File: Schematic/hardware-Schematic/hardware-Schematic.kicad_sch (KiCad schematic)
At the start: 22 parts, among them J1 DC 5V Input, Q1 NDP6020P, U1 ATmega328P-P, U14 YP-05, U16 DFPlayer, U17 MP1584, U2 HW-084

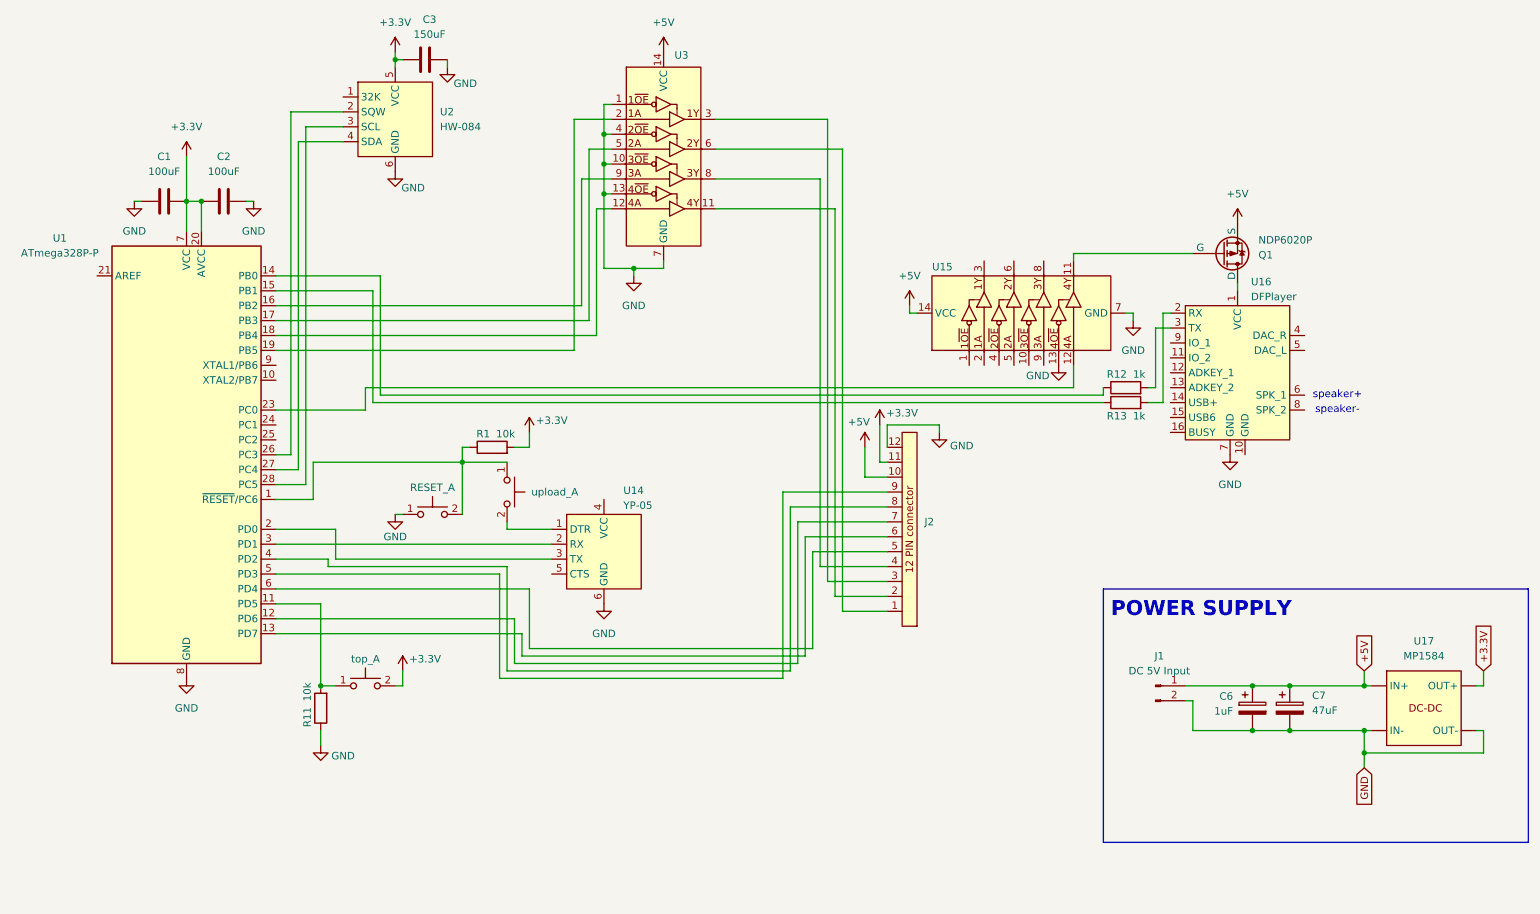
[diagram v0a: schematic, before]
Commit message: Making the hardware schematic ready for PCB implementation
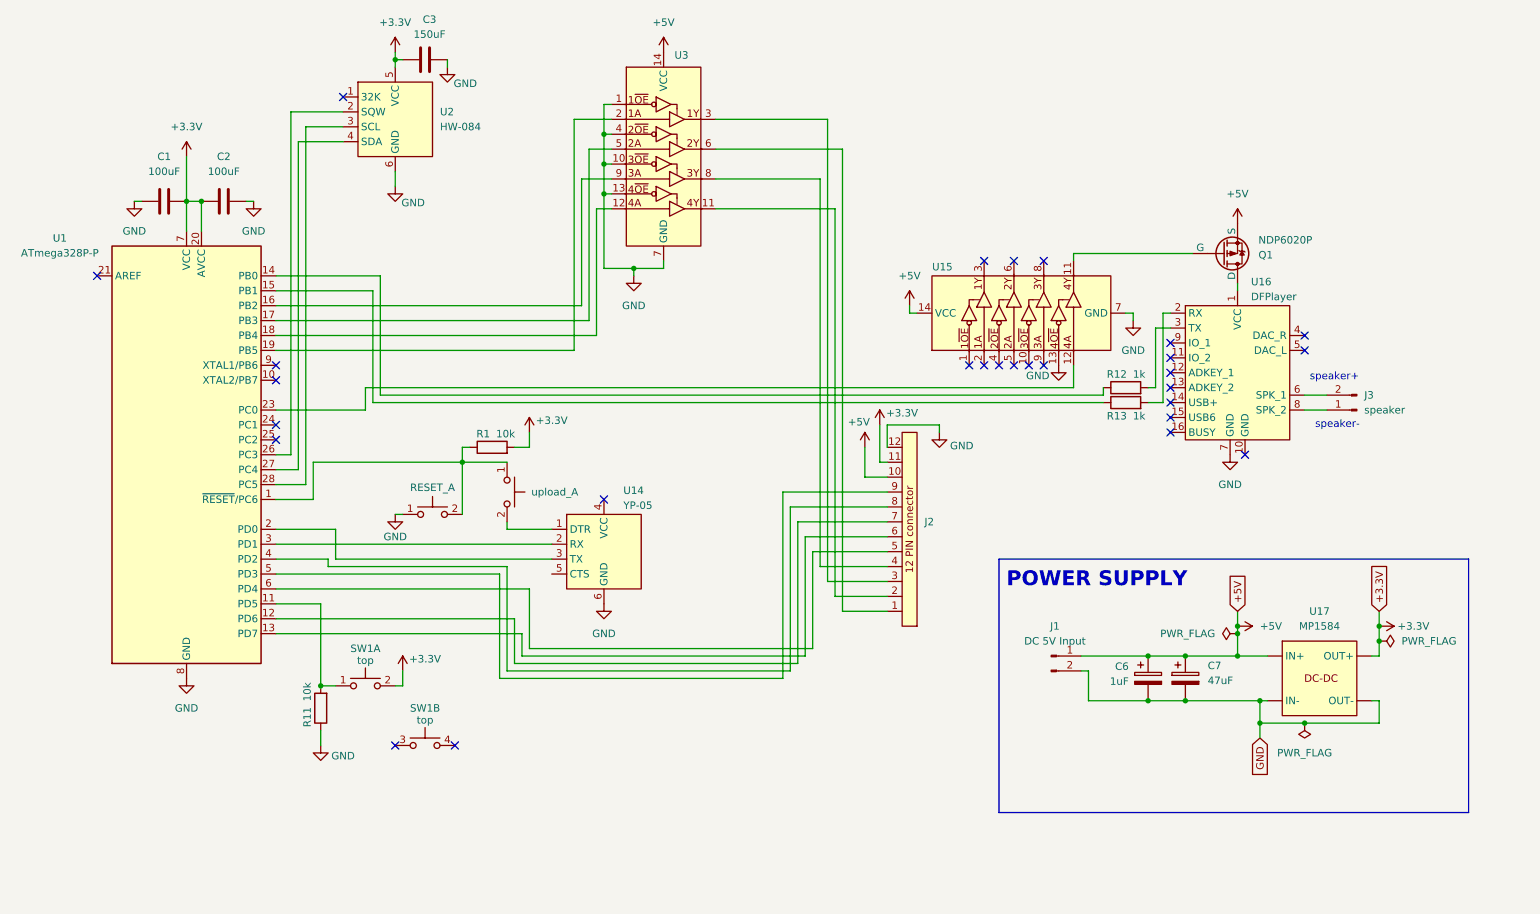
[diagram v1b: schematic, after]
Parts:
- removed top_: SW_Push_Dual_x2, symbol Switch:SW_Push_Dual_x2
- added J3: speaker, symbol Connector:Conn_01x02_Pin
- added SW1: top, symbol Switch:SW_Push_Dual_x2
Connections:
- net +3.3V: now also SW1.2 (D)
- net at U16.6 (SPK_1): now also J3.2 (Pin_2)
- net at U16.8 (SPK_2): now also J3.1 (Pin_1)
- net at R11.2, U1.11 (PD5): now also SW1.1 (C)
- no-connect marks 0 -> 28
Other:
- moved on the sheet: C6, C7, J1, U17

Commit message: USC-C to 5V DC plug added to custom lib
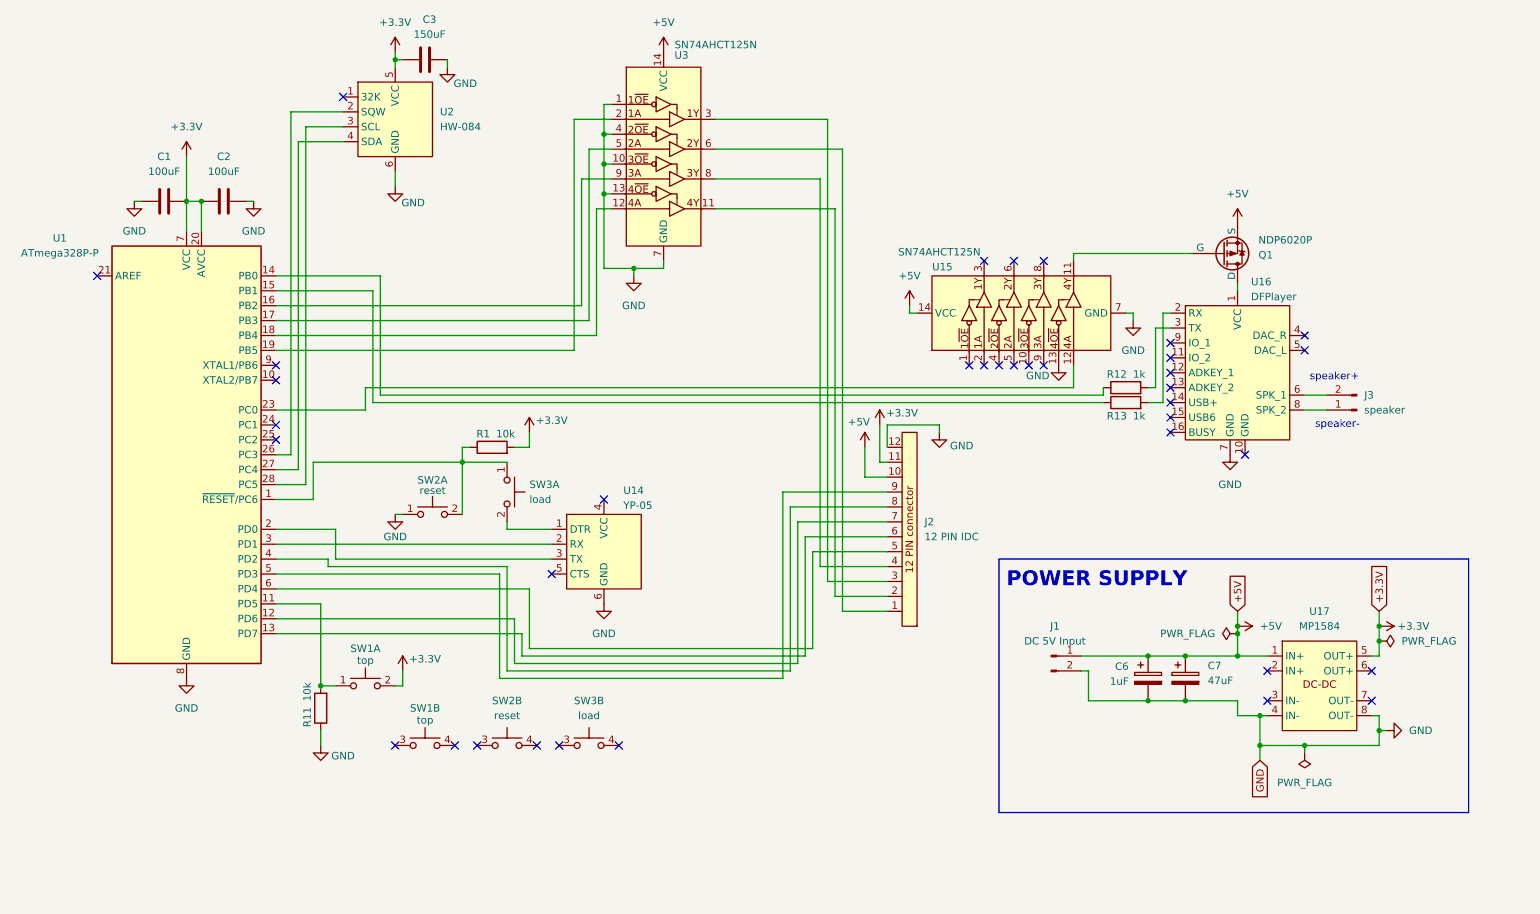
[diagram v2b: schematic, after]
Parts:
- removed RESET_, upload_: SW_Push_Dual_x2, symbol Switch:SW_Push_Dual_x2
- added SW2: reset, symbol Switch:SW_Push_Dual_x2
- added SW3: load, symbol Switch:SW_Push_Dual_x2
- C1, C2: footprint (none) -> Capacitor_THT:C_Axial_L12.0mm_D6.5mm_P15.00mm_Horizontal
- C3: footprint (none) -> Capacitor_THT:C_Rect_L7.2mm_W3.0mm_P5.00mm_FKS2_FKP2_MKS2_MKP2
- C6, C7: footprint (none) -> Capacitor_THT:CP_Radial_D5.0mm_P2.50mm
- J2: value ~ -> 12 PIN IDC
- U15, U3: value ~ -> SN74AHCT125N
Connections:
- net +3.3V: now also U17.5 (OUT+); no longer U17. (OUT+)
- net +5V: now also U17.1 (IN+); no longer U17. (OUT+)
- net GND: now also U17.4 (IN-), U17.8 (OUT-), SW2.1 (C); no longer U17. (OUT+)
- net at R1.1, U1.1 (~{RESET}/PC6): now also SW2.2 (D), SW3.1 (C)
- net at U14.1 (DTR): now also SW3.2 (D)
- no-connect marks 28 -> 37

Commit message: created pcb part for hardware size, all object, but still need layout and connections
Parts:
- J1: footprint (none) -> CustomFootprintLib:USB-C DC input 5V
- J2: footprint (none) -> Connector_IDC:IDC-Header_2x06_P2.54mm_Vertical
- J3: footprint (none) -> CustomFootprintLib:TopButton
- Q1: footprint (none) -> Package_TO_SOT_THT:TO-220F-3_Vertical
- R1, R11, R12, R13: footprint (none) -> Resistor_THT:R_Axial_DIN0207_L6.3mm_D2.5mm_P10.16mm_Horizontal
- SW1, SW2, SW3: footprint (none) -> Button_Switch_THT:SW_PUSH_6mm
- U14, U2: footprint (none) -> CustomFootprintLib:HW-084_YP-05
- U15, U3: footprint (none) -> Package_DIP:DIP-14_W7.62mm
- U16: footprint (none) -> CustomFootprintLib:DFPlayer
- U17: footprint (none) -> CustomFootprintLib:MP1584
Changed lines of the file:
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@@
 			)
 		)
-		(property "Footprint" ""
+		(property "Footprint" "CustomFootprintLib:DFPlayer"
 			(at 228.6 67.31 0)
 			(effects
@@
 			)
 		)
-		(property "Footprint" ""
+		(property "Footprint" "Button_Switch_THT:SW_PUSH_6mm"
 			(at 104.14 137.16 0)
 			(effects
@@
 			)
 		)
-		(property "Footprint" ""
+		(property "Footprint" "Resistor_THT:R_Axial_DIN0207_L6.3mm_D2.5mm_P10.16mm_Horizontal"
 			(at 101.6 93.218 90)
 			(effects
@@
 			)
 		)
-		(property "Footprint" ""
+		(property "Footprint" "CustomFootprintLib:MP1584"
 			(at 242.57 124.46 0)
 			(effects
@@
 			)
 		)
-		(property "Footprint" ""
+		(property "Footprint" "Package_TO_SOT_THT:TO-220F-3_Vertical"
 			(at 231.14 60.96 0)
 			(effects
@@
 			)
 		)
-		(property "Footprint" ""
+		(property "Footprint" "Button_Switch_THT:SW_PUSH_6mm"
 			(at 80.01 127 0)
 			(effects
@@
 			)
 		)
-		(property "Footprint" ""
+		(property "Footprint" "Resistor_THT:R_Axial_DIN0207_L6.3mm_D2.5mm_P10.16mm_Horizontal"
 			(at 209.55 85.598 90)
 			(effects
@@
 			)
 		)
-		(property "Footprint" ""
+		(property "Footprint" "CustomFootprintLib:HW-084_YP-05"
 			(at 120.65 102.87 0)
 			(effects
@@
 			)
 		)
-		(property "Footprint" ""
+		(property "Footprint" "Package_DIP:DIP-14_W7.62mm"
 			(at 171.45 68.58 0)
 			(effects
@@
 			)
 		)
-		(property "Footprint" ""
+		(property "Footprint" "Resistor_THT:R_Axial_DIN0207_L6.3mm_D2.5mm_P10.16mm_Horizontal"
 			(at 74.168 135.89 90)
 			(effects
@@
 			)
 		)
-		(property "Footprint" ""
+		(property "Footprint" "Resistor_THT:R_Axial_DIN0207_L6.3mm_D2.5mm_P10.16mm_Horizontal"
 			(at 209.55 83.058 90)
 			(effects
@@
 			)
 		)
-		(property "Footprint" ""
+		(property "Footprint" "CustomFootprintLib:HW-084_YP-05"
 			(at 85.09 29.21 0)
 			(effects
@@
 			)
 		)
-		(property "Footprint" ""
+		(property "Footprint" "Button_Switch_THT:SW_PUSH_6mm"
 			(at 109.22 99.06 0)
 			(effects
@@
 			)
 		)
-		(property "Footprint" ""
+		(property "Footprint" "Button_Switch_THT:SW_PUSH_6mm"
 			(at 118.11 137.16 0)
 			(effects
@@
 			)
 		)
-		(property "Footprint" ""
+		(property "Footprint" "Package_DIP:DIP-14_W7.62mm"
 			(at 130.81 21.59 0)
 			(effects
@@
 			)
 		)
-		(property "Footprint" ""
+		(property "Footprint" "Connector_IDC:IDC-Header_2x06_P2.54mm_Vertical"
 			(at 172.72 121.92 0)
 			(effects
@@
 			)
 		)
-		(property "Footprint" ""
+		(property "Footprint" "CustomFootprintLib:TopButton"
 			(at 248.92 85.09 0)
 			(effects
@@
 			)
 		)
-		(property "Footprint" ""
+		(property "Footprint" "Button_Switch_THT:SW_PUSH_6mm"
 			(at 90.17 137.16 0)
 			(effects
@@
 			)
 		)
-		(property "Footprint" ""
+		(property "Footprint" "CustomFootprintLib:USB-C DC input 5V"
 			(at 196.85 127 0)
 			(effects
@@
 			)
 		)
-		(property "Footprint" ""
+		(property "Footprint" "Button_Switch_THT:SW_PUSH_6mm"
 			(at 91.44 97.79 0)
 			(effects

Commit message: started the rooting but some thing moved and now every thing is miss placed I must start from the beginning again
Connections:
- net +3.3V: now also U17.8 (OUT+); no longer U17.5 (OUT+)
- net GND: now also U17.5 (OUT-); no longer U17.8 (OUT-)

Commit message: Further work on the hardware side of the pcb
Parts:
- removed unit 1 of SW1
- added J4: Conn_01x02_Pin, symbol Connector:Conn_01x02_Pin
- added R10, R6, R7, R8, R9: 10k, Resistor_THT:R_Axial_DIN0207_L6.3mm_D2.5mm_P10.16mm_Horizontal, symbol Device:R
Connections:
- net +3.3V: now also J2.6, J4.1 (Pin_1); no longer J2.11
- net +5V: now also J2.7; no longer J2.10
- net GND: now also R10.1, R6.1, R7.1, R8.1, R9.1
- net at R11.2, U1.11 (PD5): now also J4.2 (Pin_2)
- net at U15.12: now also U1.9 (XTAL1/PB6); no longer U1.23 (PC0)
- net at J2.2: now also U1.5 (PD3), R6.2; no longer U3.11
- net at U3.12: now also U1.19 (PB5); no longer U1.18 (PB4)
- net at U3.2: now also U1.16 (PB2); no longer U1.19 (PB5)
- net at J2.3: now also U1.12 (PD6), R8.2; no longer U3.3
- net at J2.1: now also U1.13 (PD7), R9.2; no longer U3.6
- net at J2.4: now also U1.6 (PD4), R10.2; no longer U3.8
- net at U3.9: now also U1.18 (PB4); no longer U1.16 (PB2)
- net at U1.4 (PD2): now also J2.5, R7.2; no longer J2.8
- net at J2.9: now also U3.6; no longer U1.5 (PD3)
- new net: J2.11, U3.11
- new net: J2.8, U3.3
- new net: J2.10, U3.8

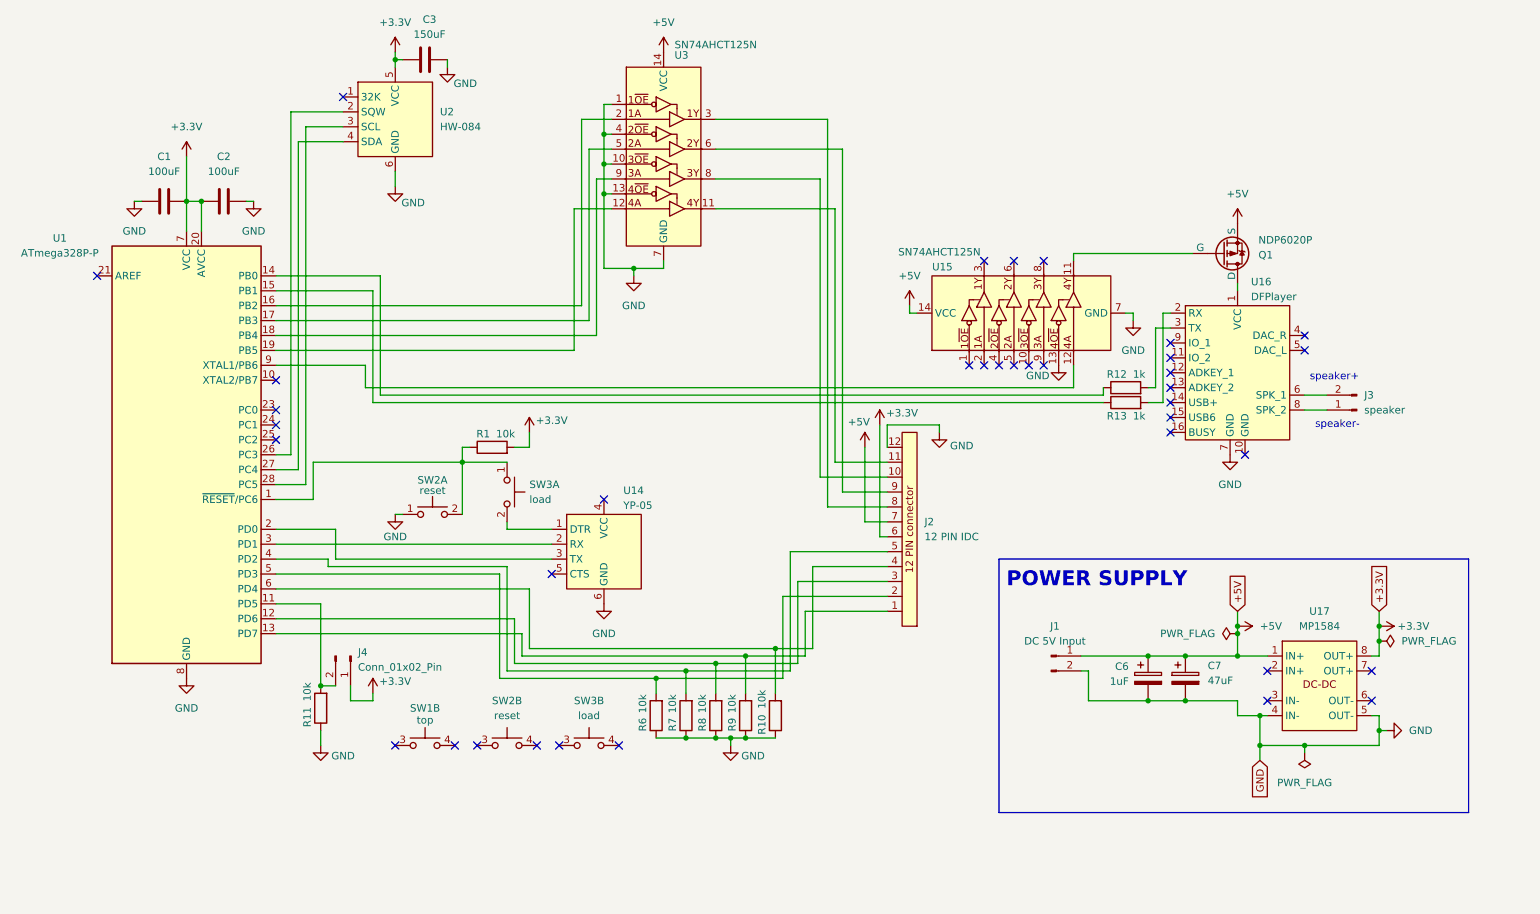
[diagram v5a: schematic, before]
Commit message: Finished the PCBs. I had to use two jumper cable. I also adjusted the position of some traces close to pins
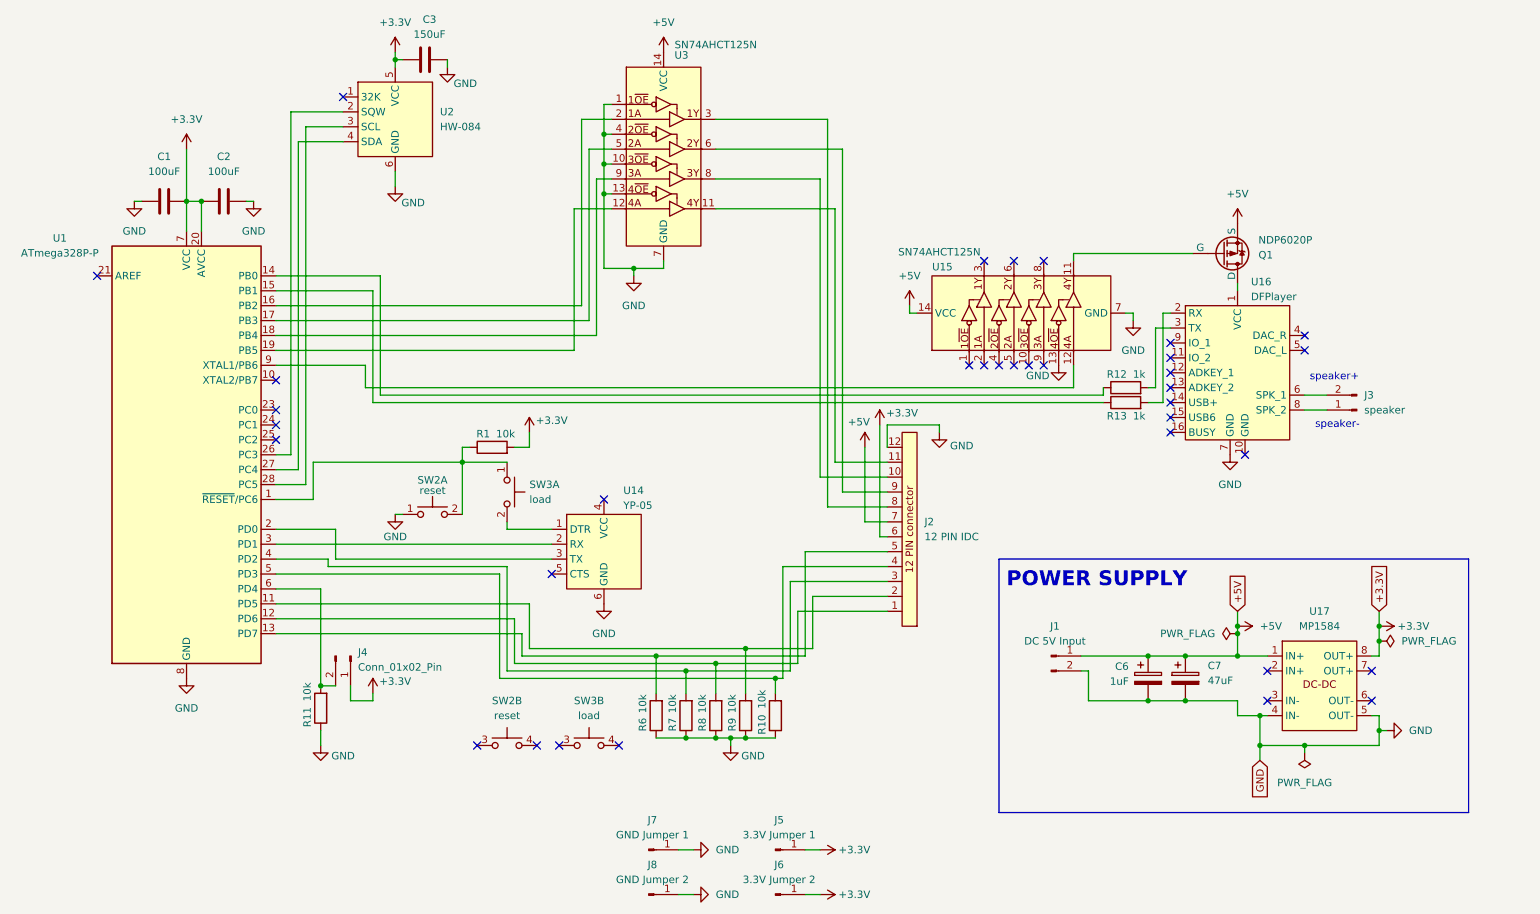
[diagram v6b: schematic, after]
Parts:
- removed SW1: top, Button_Switch_THT:SW_PUSH_6mm, symbol Switch:SW_Push_Dual_x2
- added J5: 3.3V Jumper 1, Connector_Pin:Pin_D0.7mm_L6.5mm_W1.8mm_FlatFork, symbol Connector:Conn_01x01_Pin
- added J6: 3.3V Jumper 2, Connector_Pin:Pin_D0.7mm_L6.5mm_W1.8mm_FlatFork, symbol Connector:Conn_01x01_Pin
- added J7: GND Jumper 1, Connector_Pin:Pin_D0.7mm_L6.5mm_W1.8mm_FlatFork, symbol Connector:Conn_01x01_Pin
- added J8: GND Jumper 2, Connector_Pin:Pin_D0.7mm_L6.5mm_W1.8mm_FlatFork, symbol Connector:Conn_01x01_Pin
- J4: footprint (none) -> Resistor_THT:R_Axial_DIN0207_L6.3mm_D2.5mm_P10.16mm_Horizontal
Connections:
- net +3.3V: now also J5.1 (Pin_1), J6.1 (Pin_1)
- net GND: now also J7.1 (Pin_1), J8.1 (Pin_1)
- net at J2.4, R10.2: now also U1.5 (PD3); no longer U1.6 (PD4)
- net at R8.2, U1.12 (PD6): now also J2.1; no longer J2.3
- net at J4.2 (Pin_2), R11.2: now also U1.6 (PD4); no longer U1.11 (PD5)
- net at R7.2, U1.4 (PD2): now also J2.3; no longer J2.5
- new net: J2.2, R9.2, U1.11 (PD5)
- new net: J2.5, R6.2, U1.13 (PD7)
- no-connect marks 37 -> 35
